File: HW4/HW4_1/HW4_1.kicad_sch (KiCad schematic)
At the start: 23 parts, among them J1 CP2102N, J2 Battery, J3 Conn_01x12_Pin, J4 Conn_01x12_Pin, SW1 RESET, SW2 USER, SW3 SW_DPDT_x2, U1 PIC32MX170F256B, U2 AP7381-33Y

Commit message: PCB footprint & start of board
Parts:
- C1, C2, C3: footprint (none) -> Capacitor_THT:C_Disc_D5.1mm_W3.2mm_P5.00mm
- C4: value 10uF -> 1uF; footprint (none) -> Capacitor_THT:C_Disc_D5.1mm_W3.2mm_P5.00mm
- C5: footprint (none) -> Capacitor_THT:C_Disc_D3.4mm_W2.1mm_P2.50mm
- C6: value 0.1 -> 0.1 uF; footprint (none) -> Capacitor_THT:C_Disc_D3.4mm_W2.1mm_P2.50mm
- D1, D2, D3: footprint (none) -> LED_THT:LED_D3.0mm
- J1: footprint (none) -> Connector_PinHeader_2.54mm:PinHeader_1x06_P2.54mm_Vertical
- J2: footprint (none) -> Connector_PinHeader_2.54mm:PinHeader_1x02_P2.54mm_Vertical
- J3, J4: footprint (none) -> Connector_PinHeader_2.54mm:PinHeader_1x12_P2.54mm_Vertical
- R1, R2, R3, R4, R5: footprint (none) -> Resistor_THT:R_Axial_DIN0207_L6.3mm_D2.5mm_P7.62mm_Horizontal
- SW1, SW2: footprint (none) -> HW4:pushbutton
- SW3: footprint (none) -> HW4:Slideswitch
- U1: footprint (none) -> Package_DIP:DIP-28_W7.62mm_Socket
- U2: footprint Package_TO_SOT_SMD:SOT-89-3 -> Package_TO_SOT_THT:TO-92_Inline
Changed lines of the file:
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@@
       (effects (font (size 1.27 1.27)))
     )
-    (property "Footprint" "Package_TO_SOT_SMD:SOT-89-3" (at 129.54 25.4 0)
+    (property "Footprint" "Package_TO_SOT_THT:TO-92_Inline" (at 129.54 25.4 0)
       (effects (font (size 1.27 1.27) italic) hide)
     )
@@
       (effects (font (size 1.27 1.27)) (justify left))
     )
-    (property "Footprint" "" (at 79.502 151.13 90)
+    (property "Footprint" "Resistor_THT:R_Axial_DIN0207_L6.3mm_D2.5mm_P7.62mm_Horizontal" (at 79.502 151.13 90)
       (effects (font (size 1.27 1.27)) hide)
     )
@@
       (effects (font (size 1.27 1.27)) (justify left))
     )
-    (property "Footprint" "" (at 144.4752 45.72 0)
+    (property "Footprint" "Capacitor_THT:C_Disc_D5.1mm_W3.2mm_P5.00mm" (at 144.4752 45.72 0)
       (effects (font (size 1.27 1.27)) hide)
     )
@@
       (effects (font (size 1.27 1.27)) (justify left))
     )
-    (property "Footprint" "" (at 62.992 151.13 90)
+    (property "Footprint" "Resistor_THT:R_Axial_DIN0207_L6.3mm_D2.5mm_P7.62mm_Horizontal" (at 62.992 151.13 90)
       (effects (font (size 1.27 1.27)) hide)
     )
@@
       (effects (font (size 1.27 1.27)))
     )
-    (property "Footprint" "" (at 44.45 33.02 0)
+    (property "Footprint" "Connector_PinHeader_2.54mm:PinHeader_1x06_P2.54mm_Vertical" (at 44.45 33.02 0)
       (effects (font (size 1.27 1.27)) hide)
     )
@@
       (effects (font (size 1.27 1.27)))
     )
-    (property "Footprint" "" (at 241.3 52.07 0)
+    (property "Footprint" "Connector_PinHeader_2.54mm:PinHeader_1x12_P2.54mm_Vertical" (at 241.3 52.07 0)
       (effects (font (size 1.27 1.27)) hide)
     )
@@
       (effects (font (size 1.27 1.27)) (justify right))
     )
-    (property "Footprint" "" (at 64.77 137.16 0)
+    (property "Footprint" "LED_THT:LED_D3.0mm" (at 64.77 137.16 0)
       (effects (font (size 1.27 1.27)) hide)
     )
@@
       (effects (font (size 1.27 1.27)))
     )
-    (property "Footprint" "" (at 170.2779 103.9207 0)
+    (property "Footprint" "Package_DIP:DIP-28_W7.62mm_Socket" (at 170.2779 103.9207 0)
       (effects (font (size 1.27 1.27)) hide)
     )
@@
       (effects (font (size 1.27 1.27)))
     )
-    (property "Footprint" "" (at 201.93 52.07 0)
+    (property "Footprint" "Connector_PinHeader_2.54mm:PinHeader_1x12_P2.54mm_Vertical" (at 201.93 52.07 0)
       (effects (font (size 1.27 1.27)) hide)
     )
@@
       (effects (font (size 1.27 1.27)) (justify right))
     )
-    (property "Footprint" "" (at 81.28 137.16 0)
+    (property "Footprint" "LED_THT:LED_D3.0mm" (at 81.28 137.16 0)
       (effects (font (size 1.27 1.27)) hide)
     )
@@
       (effects (font (size 1.27 1.27)))
     )
-    (property "Footprint" "" (at 82.55 118.618 90)
+    (property "Footprint" "Resistor_THT:R_Axial_DIN0207_L6.3mm_D2.5mm_P7.62mm_Horizontal" (at 82.55 118.618 90)
       (effects (font (size 1.27 1.27)) hide)
     )
@@
       (effects (font (size 1.27 1.27)) (justify left))
     )
-    (property "Footprint" "" (at 113.9952 45.72 0)
+    (property "Footprint" "Capacitor_THT:C_Disc_D5.1mm_W3.2mm_P5.00mm" (at 113.9952 45.72 0)
       (effects (font (size 1.27 1.27)) hide)
     )
@@
       (effects (font (size 1.27 1.27)) (justify left))
     )
-    (property "Footprint" "" (at 135.5852 129.54 0)
+    (property "Footprint" "Capacitor_THT:C_Disc_D3.4mm_W2.1mm_P2.50mm" (at 135.5852 129.54 0)
       (effects (font (size 1.27 1.27)) hide)
     )
@@
       (effects (font (size 1.27 1.27)) (justify right))
     )
-    (property "Footprint" "" (at 170.688 41.91 90)
+    (property "Footprint" "Resistor_THT:R_Axial_DIN0207_L6.3mm_D2.5mm_P7.62mm_Horizontal" (at 170.688 41.91 90)
       (effects (font (size 1.27 1.27)) hide)
     )
@@
       (effects (font (size 1.27 1.27)))
     )
-    (property "Footprint" "" (at 82.55 97.028 90)
+    (property "Footprint" "Resistor_THT:R_Axial_DIN0207_L6.3mm_D2.5mm_P7.62mm_Horizontal" (at 82.55 97.028 90)
       (effects (font (size 1.27 1.27)) hide)
     )
@@
       (effects (font (size 1.27 1.27)))
     )
-    (property "Footprint" "" (at 45.72 58.42 0)
+    (property "Footprint" "Connector_PinHeader_2.54mm:PinHeader_1x02_P2.54mm_Vertical" (at 45.72 58.42 0)
       (effects (font (size 1.27 1.27)) hide)
     )
@@
       (effects (font (size 1.27 1.27)))
     )
-    (property "Footprint" "" (at 66.04 90.17 0)
+    (property "Footprint" "HW4:pushbutton" (at 66.04 90.17 0)
       (effects (font (size 1.27 1.27)) hide)
     )
@@
       (effects (font (size 1.27 1.27)))
     )
-    (property "Footprint" "" (at 165.1 38.1 0)
+    (property "Footprint" "LED_THT:LED_D3.0mm" (at 165.1 38.1 0)
       (effects (font (size 1.27 1.27)) hide)
     )
@@
       (effects (font (size 1.27 1.27)))
     )
-    (property "Value" "0.1" (at 208.28 97.79 90)
-      (effects (font (size 1.27 1.27)))
-    )
-    (property "Footprint" "" (at 212.09 100.6348 0)
+    (property "Value" "0.1 uF" (at 208.28 97.79 90)
+      (effects (font (size 1.27 1.27)))
+    )
+    (property "Footprint" "Capacitor_THT:C_Disc_D3.4mm_W2.1mm_P2.50mm" (at 212.09 100.6348 0)
       (effects (font (size 1.27 1.27)) hide)
     )
@@
       (effects (font (size 1.27 1.27)))
     )
-    (property "Footprint" "" (at 96.52 38.1 0)
+    (property "Footprint" "HW4:Slideswitch" (at 96.52 38.1 0)
       (effects (font (size 1.27 1.27)) hide)
     )
@@
       (effects (font (size 1.27 1.27)))
     )
-    (property "Value" "10uF" (at 199.39 118.11 90)
-      (effects (font (size 1.27 1.27)))
-    )
-    (property "Footprint" "" (at 203.2 120.9548 0)
+    (property "Value" "1uF" (at 199.39 118.11 90)
+      (effects (font (size 1.27 1.27)))
+    )
+    (property "Footprint" "Capacitor_THT:C_Disc_D5.1mm_W3.2mm_P5.00mm" (at 203.2 120.9548 0)
       (effects (font (size 1.27 1.27)) hide)
     )
@@
       (effects (font (size 1.27 1.27)))
     )
-    (property "Footprint" "" (at 66.04 111.76 0)
+    (property "Footprint" "HW4:pushbutton" (at 66.04 111.76 0)
       (effects (font (size 1.27 1.27)) hide)
     )
@@
       (effects (font (size 1.27 1.27)) (justify left))
     )
-    (property "Footprint" "" (at 154.6352 45.72 0)
-      (effects (font (size 1.27 1.27)) hide)
-    )
+    (property "Footprint" "Capacitor_THT:C_Disc_D5.1mm_W3.2mm_P5.00mm" (at 154.6352 45.72 0)
+      (effects (font (size 1.27 1.27)) hide)
+    )

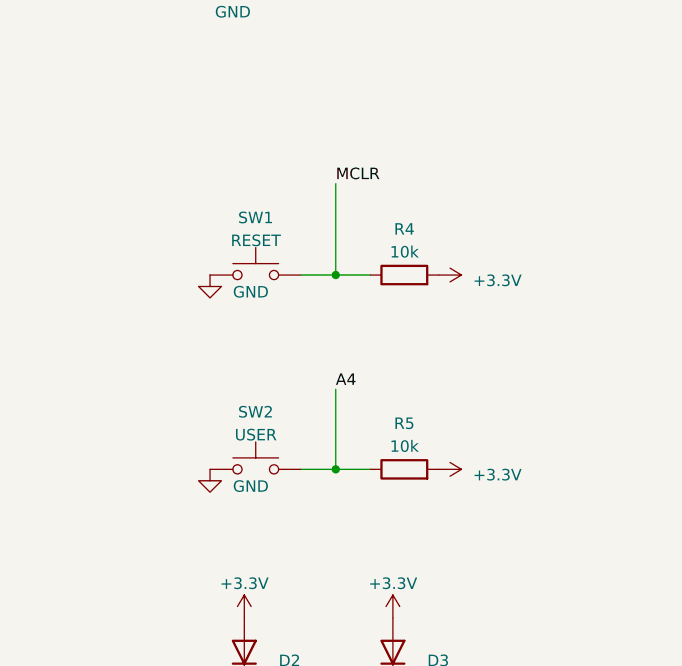
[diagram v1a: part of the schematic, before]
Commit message: board start routing
Bug to resolve: Pushbuttons have both pins GND, but assigned correctly in schematic
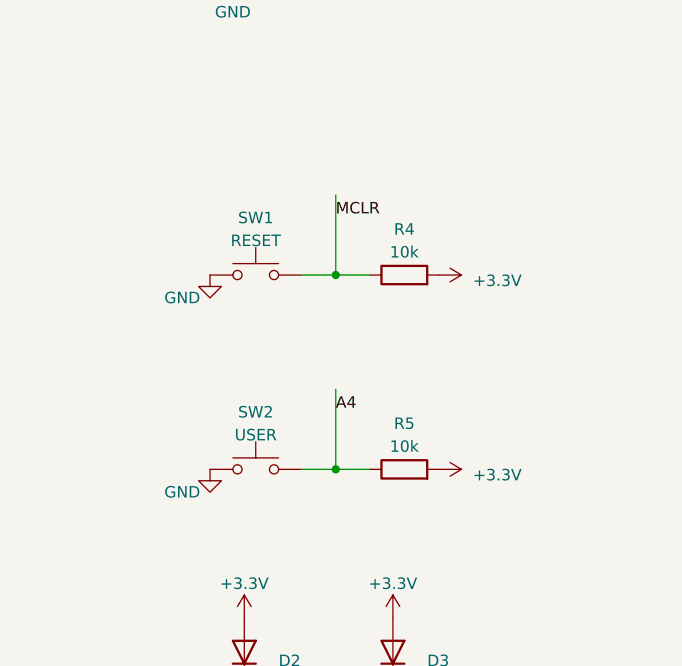
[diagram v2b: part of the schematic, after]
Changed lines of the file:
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@@
 (kicad_sch (version 20230121) (generator eeschema)
   (paper "A4")
+  (junction (at 134.62 119.38) (diameter 0) (color 0 0 0 0)
+  )
+  (junction (at 143.51 38.1) (diameter 0) (color 0 0 0 0)
+  )
+  (junction (at 195.58 101.6) (diameter 0) (color 0 0 0 0)
+  )
   (junction (at 74.93 95.25) (diameter 0) (color 0 0 0 0)
   )
-  (junction (at 134.62 119.38) (diameter 0) (color 0 0 0 0)
-  )
-  (junction (at 143.51 38.1) (diameter 0) (color 0 0 0 0)
-  )
-  (junction (at 195.58 101.6) (diameter 0) (color 0 0 0 0)
-  )
   (junction (at 212.09 104.14) (diameter 0) (color 0 0 0 0)
   )
@@
     (stroke (width 0) (type default))
   )
+  (wire (pts (xy 74.93 95.25) (xy 78.74 95.25))
+    (stroke (width 0) (type default))
+  )
   (wire (pts (xy 149.86 114.3) (xy 160.02 114.3))
     (stroke (width 0) (type default))
   )
-  (wire (pts (xy 74.93 85.09) (xy 74.93 95.25))
-    (stroke (width 0) (type default))
-  )
   (wire (pts (xy 149.86 111.76) (xy 160.02 111.76))
     (stroke (width 0) (type default))
@@
     (stroke (width 0) (type default))
   )
+  (wire (pts (xy 246.38 62.23) (xy 257.81 62.23))
+    (stroke (width 0) (type default))
+  )
+  (wire (pts (xy 207.01 44.45) (xy 218.44 44.45))
+    (stroke (width 0) (type default))
+  )
+  (wire (pts (xy 246.38 57.15) (xy 257.81 57.15))
+    (stroke (width 0) (type default))
+  )
+  (wire (pts (xy 207.01 39.37) (xy 218.44 39.37))
+    (stroke (width 0) (type default))
+  )
+  (wire (pts (xy 207.01 62.23) (xy 218.44 62.23))
+    (stroke (width 0) (type default))
+  )
+  (wire (pts (xy 83.82 35.56) (xy 91.44 35.56))
+    (stroke (width 0) (type default))
+  )
+  (wire (pts (xy 182.88 129.54) (xy 191.77 129.54))
+    (stroke (width 0) (type default))
+  )
+  (wire (pts (xy 182.88 106.68) (xy 191.77 106.68))
+    (stroke (width 0) (type default))
+  )
   (wire (pts (xy 71.12 95.25) (xy 74.93 95.25))
     (stroke (width 0) (type default))
   )
-  (wire (pts (xy 246.38 62.23) (xy 257.81 62.23))
-    (stroke (width 0) (type default))
-  )
-  (wire (pts (xy 207.01 44.45) (xy 218.44 44.45))
-    (stroke (width 0) (type default))
-  )
-  (wire (pts (xy 246.38 57.15) (xy 257.81 57.15))
-    (stroke (width 0) (type default))
-  )
-  (wire (pts (xy 207.01 39.37) (xy 218.44 39.37))
-    (stroke (width 0) (type default))
-  )
-  (wire (pts (xy 207.01 62.23) (xy 218.44 62.23))
-    (stroke (width 0) (type default))
-  )
-  (wire (pts (xy 83.82 35.56) (xy 91.44 35.56))
-    (stroke (width 0) (type default))
-  )
-  (wire (pts (xy 182.88 129.54) (xy 191.77 129.54))
-    (stroke (width 0) (type default))
-  )
-  (wire (pts (xy 182.88 106.68) (xy 191.77 106.68))
-    (stroke (width 0) (type default))
-  )
-  (wire (pts (xy 74.93 95.25) (xy 78.74 95.25))
-    (stroke (width 0) (type default))
-  )
   (wire (pts (xy 182.88 111.76) (xy 191.77 111.76))
     (stroke (width 0) (type default))
@@
     (stroke (width 0) (type default))
   )
+  (wire (pts (xy 246.38 59.69) (xy 257.81 59.69))
+    (stroke (width 0) (type default))
+  )
+  (wire (pts (xy 246.38 54.61) (xy 257.81 54.61))
+    (stroke (width 0) (type default))
+  )
+  (wire (pts (xy 74.93 107.95) (xy 74.93 116.84))
+    (stroke (width 0) (type default))
+  )
+  (wire (pts (xy 207.01 54.61) (xy 218.44 54.61))
+    (stroke (width 0) (type default))
+  )
+  (wire (pts (xy 182.88 132.08) (xy 191.77 132.08))
+    (stroke (width 0) (type default))
+  )
   (wire (pts (xy 149.86 101.6) (xy 160.02 101.6))
     (stroke (width 0) (type default))
   )
-  (wire (pts (xy 246.38 59.69) (xy 257.81 59.69))
-    (stroke (width 0) (type default))
-  )
-  (wire (pts (xy 246.38 54.61) (xy 257.81 54.61))
-    (stroke (width 0) (type default))
-  )
-  (wire (pts (xy 74.93 107.95) (xy 74.93 116.84))
-    (stroke (width 0) (type default))
-  )
-  (wire (pts (xy 207.01 54.61) (xy 218.44 54.61))
-    (stroke (width 0) (type default))
-  )
-  (wire (pts (xy 182.88 132.08) (xy 191.77 132.08))
-    (stroke (width 0) (type default))
-  )
   (wire (pts (xy 113.03 38.1) (xy 120.65 38.1))
     (stroke (width 0) (type default))
@@
     (stroke (width 0) (type default))
   )
+  (wire (pts (xy 74.93 86.36) (xy 74.93 95.25))
+    (stroke (width 0) (type default))
+  )
   (wire (pts (xy 246.38 39.37) (xy 257.81 39.37))
     (stroke (width 0) (type default))
@@
     (effects (font (size 1.27 1.27)) (justify left bottom))
   )
+  (label "A4" (at 74.93 110.49 0) (fields_autoplaced)
+    (effects (font (size 1.27 1.27)) (justify left bottom))
+  )
   (label "SCK2-B15" (at 185.42 106.68 0) (fields_autoplaced)
     (effects (font (size 1.27 1.27)) (justify left bottom))
@@
     (effects (font (size 1.27 1.27)) (justify left bottom))
   )
+  (label "MCLR" (at 74.93 88.9 0) (fields_autoplaced)
+    (effects (font (size 1.27 1.27)) (justify left bottom))
+  )
   (label "U1RX" (at 52.07 33.02 0) (fields_autoplaced)
     (effects (font (size 1.27 1.27)) (justify left bottom))
@@
     (effects (font (size 1.27 1.27)) (justify left bottom))
   )
-  (label "MCLR" (at 74.93 85.09 0) (fields_autoplaced)
-    (effects (font (size 1.27 1.27)) (justify left bottom))
-  )
   (label "Vin" (at 106.68 38.1 0) (fields_autoplaced)
     (effects (font (size 1.27 1.27)) (justify left bottom))
@@
   )
   (label "SDA1-B9" (at 248.92 54.61 0) (fields_autoplaced)
-    (effects (font (size 1.27 1.27)) (justify left bottom))
-  )
-  (label "A4" (at 74.93 107.95 0) (fields_autoplaced)
     (effects (font (size 1.27 1.27)) (justify left bottom))
   )
@@
   )
   (symbol (lib_id "power:GND") (at 60.96 116.84 0) (unit 1)
-    (in_bom yes) (on_board yes) (dnp no) (fields_autoplaced)
+    (in_bom yes) (on_board yes) (dnp no)
     (property "Reference" "#PWR014" (at 60.96 123.19 0)
       (effects (font (size 1.27 1.27)) hide)
     )
-    (property "Value" "GND" (at 63.5 118.745 0)
+    (property "Value" "GND" (at 55.88 119.38 0)
       (effects (font (size 1.27 1.27)) (justify left))
     )
@@
   )
   (symbol (lib_id "power:GND") (at 60.96 95.25 0) (unit 1)
-    (in_bom yes) (on_board yes) (dnp no) (fields_autoplaced)
+    (in_bom yes) (on_board yes) (dnp no)
     (property "Reference" "#PWR015" (at 60.96 101.6 0)
       (effects (font (size 1.27 1.27)) hide)
     )
-    (property "Value" "GND" (at 63.5 97.155 0)
+    (property "Value" "GND" (at 55.88 97.79 0)
       (effects (font (size 1.27 1.27)) (justify left))
     )
